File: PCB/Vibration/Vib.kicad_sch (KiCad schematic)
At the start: 15 parts, among them J1 Conn_01x02_Male, J2 Conn_01x02_Male, J3 Conn_01x02_Male, J4 Conn_01x02_Male, J5 Conn_01x03_Male, J6 Conn_01x03_Male, J7 Conn_01x03_Male, U1 ROB-14538, U2 ROB-14538, U3 ROB-14538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

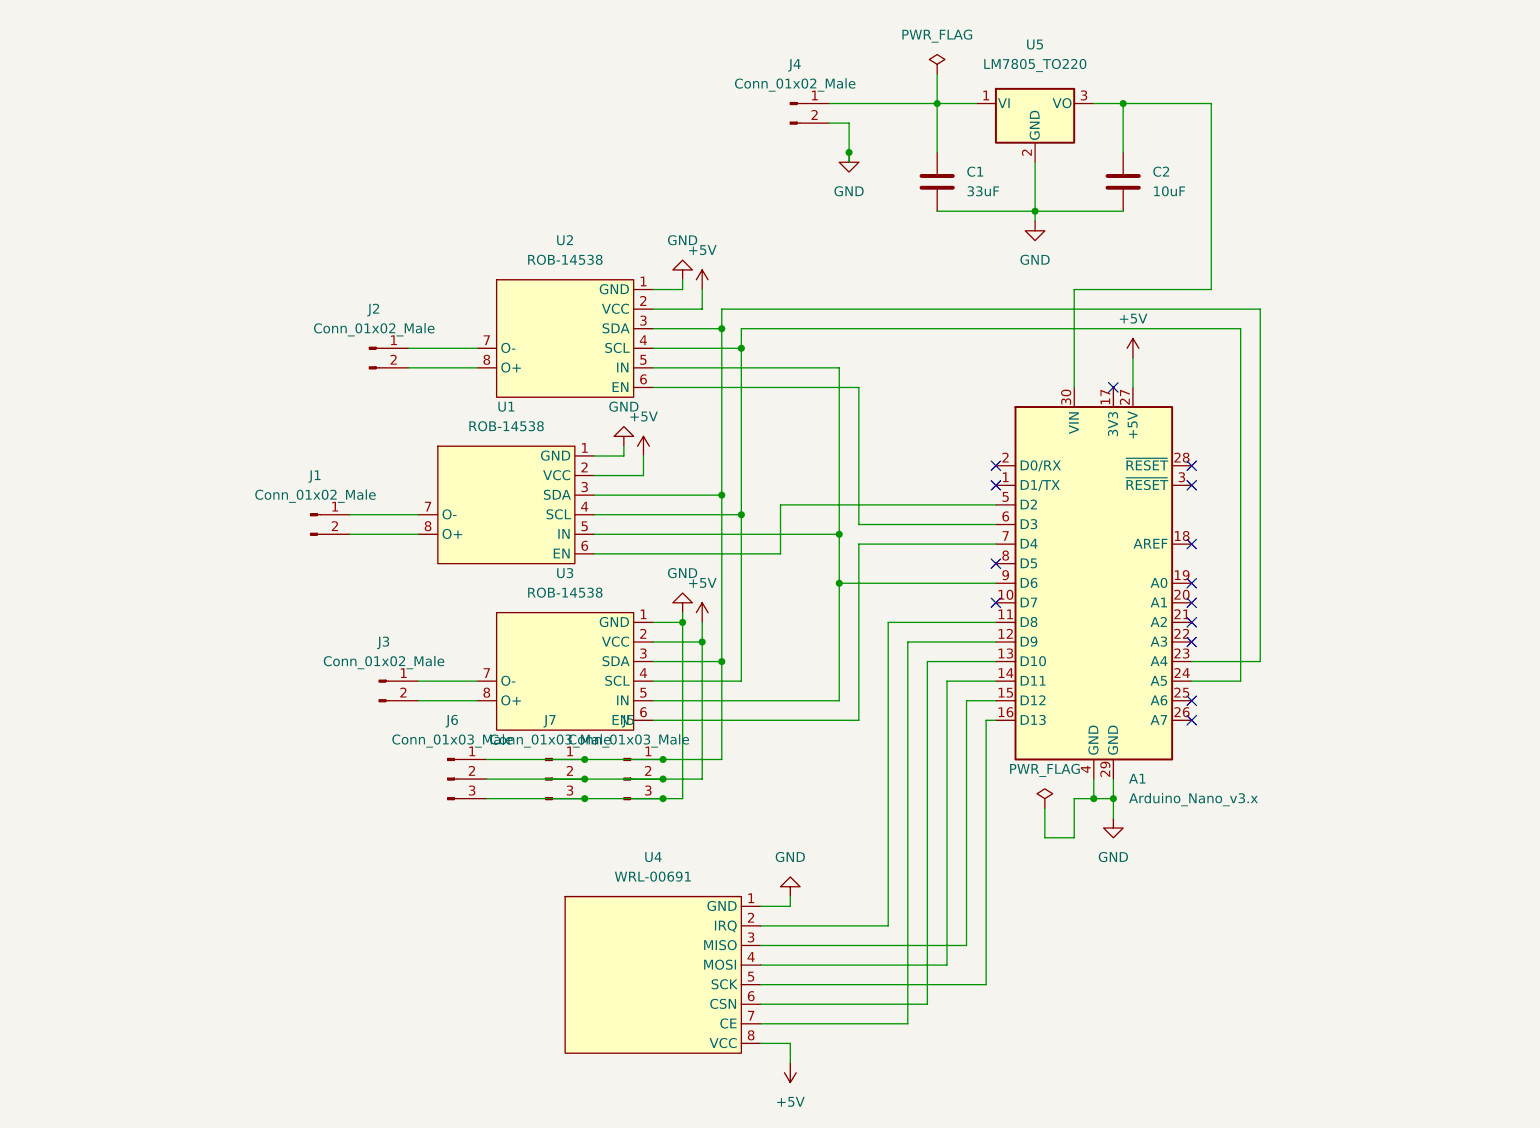
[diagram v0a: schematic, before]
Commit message: Updated PCB files; added desing files for caress and vibration
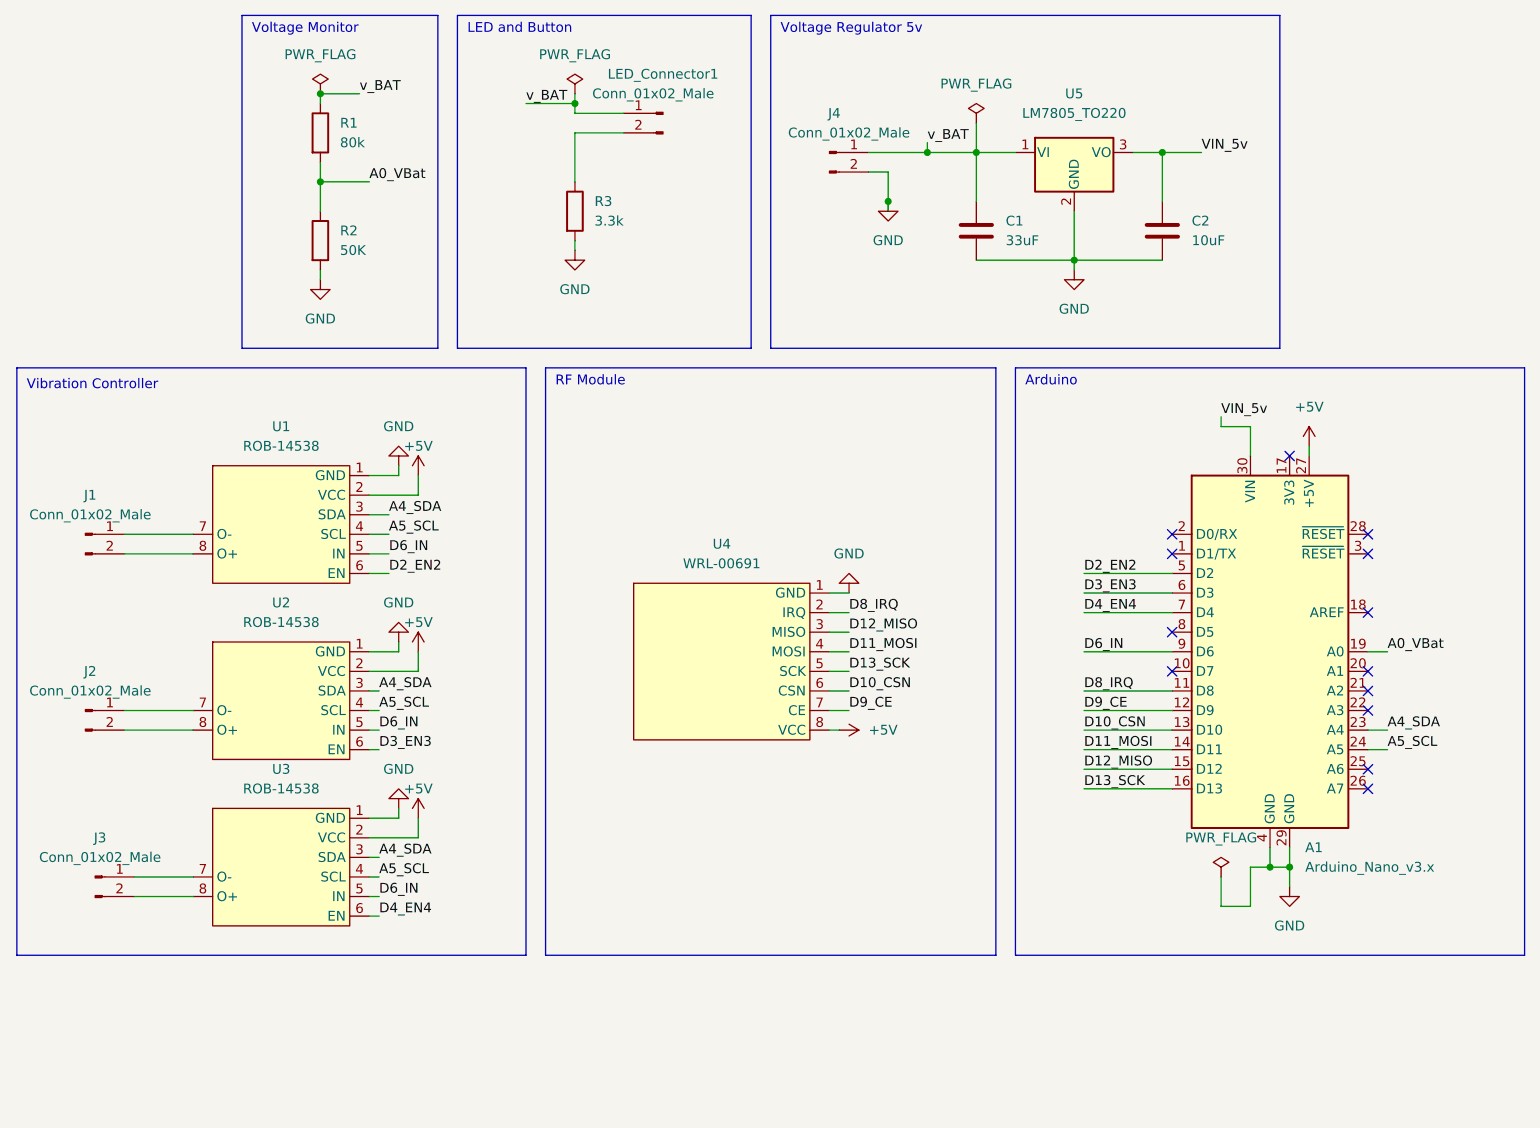
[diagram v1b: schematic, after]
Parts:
- removed J5, J6, J7: Conn_01x03_Male, Connector_PinSocket_2.54mm:PinSocket_1x03_P2.54mm_Vertical, symbol Connector:Conn_01x03_Male
- added LED_Connector1: Conn_01x02_Male, Connector_JST:JST_EH_B2B-EH-A_1x02_P2.50mm_Vertical, symbol Connector:Conn_01x02_Male
- added R1: 80k, Resistor_THT:R_Axial_DIN0207_L6.3mm_D2.5mm_P7.62mm_Horizontal, symbol Device:R
- added R2: 50K, Resistor_THT:R_Axial_DIN0207_L6.3mm_D2.5mm_P7.62mm_Horizontal, symbol Device:R
- added R3: 3.3k, Resistor_THT:R_Axial_DIN0207_L6.3mm_D2.5mm_P7.62mm_Horizontal, symbol Device:R
- C1, C2: footprint Capacitor_THT:C_Radial_D5.0mm_H11.0mm_P2.00mm -> Capacitor_THT:C_Disc_D5.0mm_W2.5mm_P5.00mm
- J1, J2, J3, J4: footprint Connector_PinSocket_2.54mm:PinSocket_1x02_P2.54mm_Vertical -> Connector_JST:JST_EH_B2B-EH-A_1x02_P2.50mm_Vertical
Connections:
- net GND: now also R2.2, R3.2
- net A4_SDA: now reaches A1.23 (A4), U1.3 (SDA), U2.3 (SDA), U3.3 (SDA)
- net A5_SCL: now reaches A1.24 (A5), U1.4 (SCL), U2.4 (SCL), U3.4 (SCL)
- net D6_IN: now reaches A1.9 (D6), U1.5 (IN), U2.5 (IN), U3.5 (IN)
- net D2_EN2: now reaches A1.5 (D2), U1.6 (EN)
- net VIN_5v: now reaches A1.30 (VIN), C2.1, U5.3 (VO)
- net v_BAT: now reaches C1.1, J4.1 (Pin_1), U5.1 (VI)
- net v_BAT: now also LED_Connector1.1 (Pin_1), R1.1
- net D8_IRQ: now reaches A1.11 (D8), U4.2 (IRQ)
- net D12_MISO: now reaches A1.15 (D12), U4.3 (MISO)
- net D11_MOSI: now reaches A1.14 (D11), U4.4 (MOSI)
- net D13_SCK: now reaches A1.16 (D13), U4.5 (SCK)
- net D10_CSN: now reaches A1.13 (D10), U4.6 (CSN)
- net D9_CE: now reaches A1.12 (D9), U4.7 (CE)
- net A0_VBat: now reaches A1.19 (A0)
- net A0_VBat: now also R1.2, R2.1
- net D3_EN3: now reaches A1.6 (D3), U2.6 (EN)
- net D4_EN4: now reaches A1.7 (D4), U3.6 (EN)
- new net: LED_Connector1.2 (Pin_2), R3.1
- no-connect marks 14 -> 13
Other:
- note added: "Arduino"
- note added: "LED and Button"
- note added: "RF Module"
- note added: "Vibration Controller"
- note added: "Voltage Monitor"
- note added: "Voltage Regulator 5v"
- moved on the sheet: A1, C1, C2, J1, J2, J3, J4, U1, U2, U3, U4, U5
